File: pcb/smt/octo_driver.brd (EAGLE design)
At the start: 34.3 x 46.2 mm, 21 parts, among them U1 LP2985-10DBVT

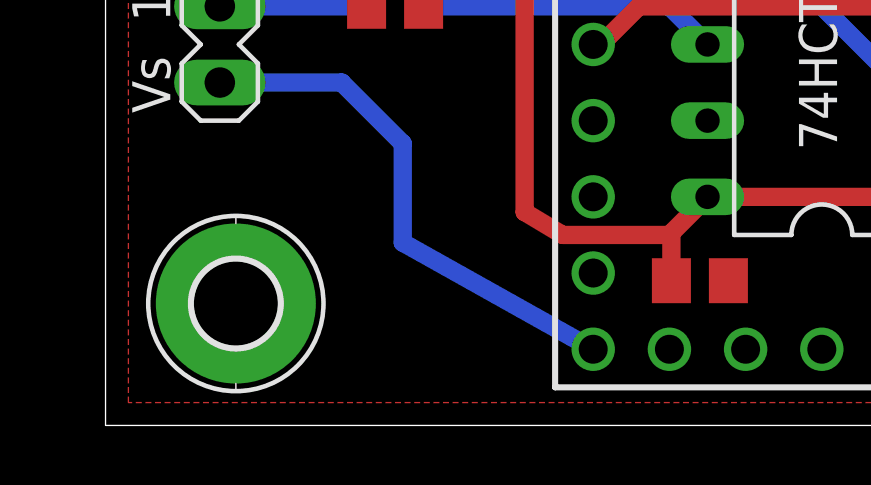
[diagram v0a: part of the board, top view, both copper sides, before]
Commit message: added test point
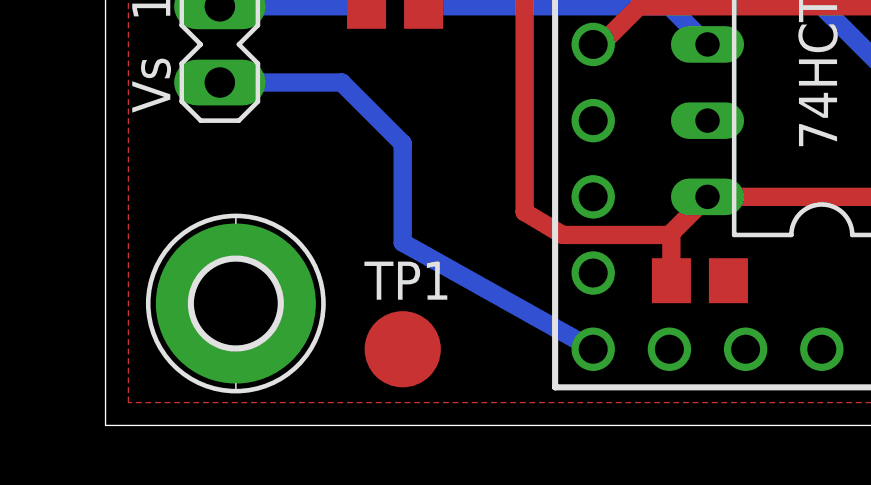
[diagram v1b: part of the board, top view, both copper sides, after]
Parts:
- added TP1: PTR1B2,54, testpad:B2,54
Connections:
- net GND: now also TP1.TP
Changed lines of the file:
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@@
 <element name="U$1" library="penrose" package="PENROSELOGO_LOWDPI" value="" x="59.436" y="69.85"/>
 <element name="U$2" library="penrose" package="PENROSELOGO_1.75IN" value="" x="44.196" y="49.276"/>
+<element name="TP1" library="testpad" package="B2,54" value="PTR1B2,54" x="45.974" y="31.496">
+<attribute name="TP_SIGNAL_NAME" value="" x="45.974" y="31.496" size="1.778" layer="27" display="off"/>
+</element>
 </elements>
 <signals>
@@
 <contactref element="H1" pad="B2,8"/>
 <contactref element="H2" pad="B2,8"/>
+<contactref element="TP1" pad="TP"/>
 </signal>
 <signal name="N$16">
@@
 <wire x1="46.67" y1="60.706" x2="54.864" y2="60.706" width="0.6096" layer="16"/>
 <wire x1="54.864" y1="60.706" x2="56.134" y2="59.436" width="0.6096" layer="16"/>
+<wire x1="46.67" y1="60.706" x2="46.67" y2="60.706" width="0" layer="19" extent="1-16"/>
 </signal>
 <signal name="N$17">
@@
 <wire x1="46.67" y1="58.166" x2="54.864" y2="58.166" width="0.6096" layer="16"/>
 <wire x1="54.864" y1="58.166" x2="56.134" y2="56.896" width="0.6096" layer="16"/>
+<wire x1="46.67" y1="58.166" x2="46.67" y2="58.166" width="0" layer="19" extent="1-16"/>
 </signal>
 <signal name="N$19">
@@
 <wire x1="52.832" y1="55.626" x2="54.102" y2="54.356" width="0.6096" layer="16"/>
 <wire x1="54.102" y1="54.356" x2="56.134" y2="54.356" width="0.6096" layer="16"/>
+<wire x1="46.67" y1="55.626" x2="46.67" y2="55.626" width="0" layer="19" extent="1-16"/>
 </signal>
 <signal name="N$20">
@@
 <wire x1="46.67" y1="53.086" x2="54.864" y2="53.086" width="0.6096" layer="16"/>
 <wire x1="54.864" y1="53.086" x2="56.134" y2="51.816" width="0.6096" layer="16"/>
+<wire x1="46.67" y1="53.086" x2="46.67" y2="53.086" width="0" layer="19" extent="1-16"/>
 </signal>
 <signal name="N$21">
@@
 <wire x1="46.67" y1="50.546" x2="54.864" y2="50.546" width="0.6096" layer="16"/>
 <wire x1="54.864" y1="50.546" x2="56.134" y2="49.276" width="0.6096" layer="16"/>
+<wire x1="46.67" y1="50.546" x2="46.67" y2="50.546" width="0" layer="19" extent="1-16"/>
 </signal>
 <signal name="N$22">
@@
 <wire x1="46.67" y1="48.006" x2="54.864" y2="48.006" width="0.6096" layer="16"/>
 <wire x1="54.864" y1="48.006" x2="56.134" y2="46.736" width="0.6096" layer="16"/>
+<wire x1="46.67" y1="48.006" x2="46.67" y2="48.006" width="0" layer="19" extent="1-16"/>
 </signal>
 <signal name="N$23">
@@
 <wire x1="46.67" y1="45.466" x2="54.864" y2="45.466" width="0.6096" layer="16"/>
 <wire x1="54.864" y1="45.466" x2="56.134" y2="44.196" width="0.6096" layer="16"/>
+<wire x1="46.67" y1="45.466" x2="46.67" y2="45.466" width="0" layer="19" extent="1-16"/>
 </signal>
 <signal name="N$24">
@@
 <wire x1="46.67" y1="42.926" x2="54.864" y2="42.926" width="0.6096" layer="16"/>
 <wire x1="54.864" y1="42.926" x2="56.134" y2="41.656" width="0.6096" layer="16"/>
+<wire x1="46.67" y1="42.926" x2="46.67" y2="42.926" width="0" layer="19" extent="1-16"/>
 </signal>
 <signal name="LED7_3.3">
@@
 <contactref element="SV1" pad="2"/>
 <wire x1="44.77" y1="42.926" x2="39.878" y2="42.926" width="0.6096" layer="16"/>
+<wire x1="44.77" y1="42.926" x2="44.77" y2="42.926" width="0" layer="19" extent="1-16"/>
 </signal>
 <signal name="LED2_3.3">
@@
 <contactref element="SV1" pad="3"/>
 <wire x1="39.878" y1="45.466" x2="44.77" y2="45.466" width="0.6096" layer="16"/>
+<wire x1="44.77" y1="45.466" x2="44.77" y2="45.466" width="0" layer="19" extent="1-16"/>
 </signal>
 <signal name="LED3">
@@
 <contactref element="SV1" pad="4"/>
 <wire x1="44.77" y1="48.006" x2="39.878" y2="48.006" width="0.6096" layer="16"/>
+<wire x1="44.77" y1="48.006" x2="44.77" y2="48.006" width="0" layer="19" extent="1-16"/>
 </signal>
 <signal name="LED4">
@@
 <contactref element="SV1" pad="5"/>
 <wire x1="39.878" y1="50.546" x2="44.77" y2="50.546" width="0.6096" layer="16"/>
+<wire x1="44.77" y1="50.546" x2="44.77" y2="50.546" width="0" layer="19" extent="1-16"/>
 </signal>
 <signal name="LED5">
@@
 <contactref element="SV1" pad="6"/>
 <wire x1="44.77" y1="53.086" x2="39.878" y2="53.086" width="0.6096" layer="16"/>
+<wire x1="44.77" y1="53.086" x2="44.77" y2="53.086" width="0" layer="19" extent="1-16"/>
 </signal>
 <signal name="LED6">
@@
 <contactref element="SV1" pad="7"/>
 <wire x1="39.878" y1="55.626" x2="44.77" y2="55.626" width="0.6096" layer="16"/>
+<wire x1="44.77" y1="55.626" x2="44.77" y2="55.626" width="0" layer="19" extent="1-16"/>
 </signal>
 <signal name="LED7">
@@
 <contactref element="SV1" pad="8"/>
 <wire x1="44.77" y1="58.166" x2="39.878" y2="58.166" width="0.6096" layer="16"/>
+<wire x1="44.77" y1="58.166" x2="44.77" y2="58.166" width="0" layer="19" extent="1-16"/>
 </signal>
 <signal name="LED8">
@@
 <contactref element="SV1" pad="9"/>
 <wire x1="39.878" y1="60.706" x2="44.77" y2="60.706" width="0.6096" layer="16"/>
+<wire x1="44.77" y1="60.706" x2="44.77" y2="60.706" width="0" layer="19" extent="1-16"/>
 </signal>
 <signal name="LED1_3.3">
